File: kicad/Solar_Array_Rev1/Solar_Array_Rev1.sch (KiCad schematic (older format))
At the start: 36 parts, among them IC1 TVS_4x4, IC2 SPV1040, IC3 LTC2990.1, IC4 TVS_4x4, P1 PV_IN, P2 CONN_01X07, Q1 Q_NMOS_DGS, Q2 Q_PMOS_DGS, Q3 Q_NPN_BCE

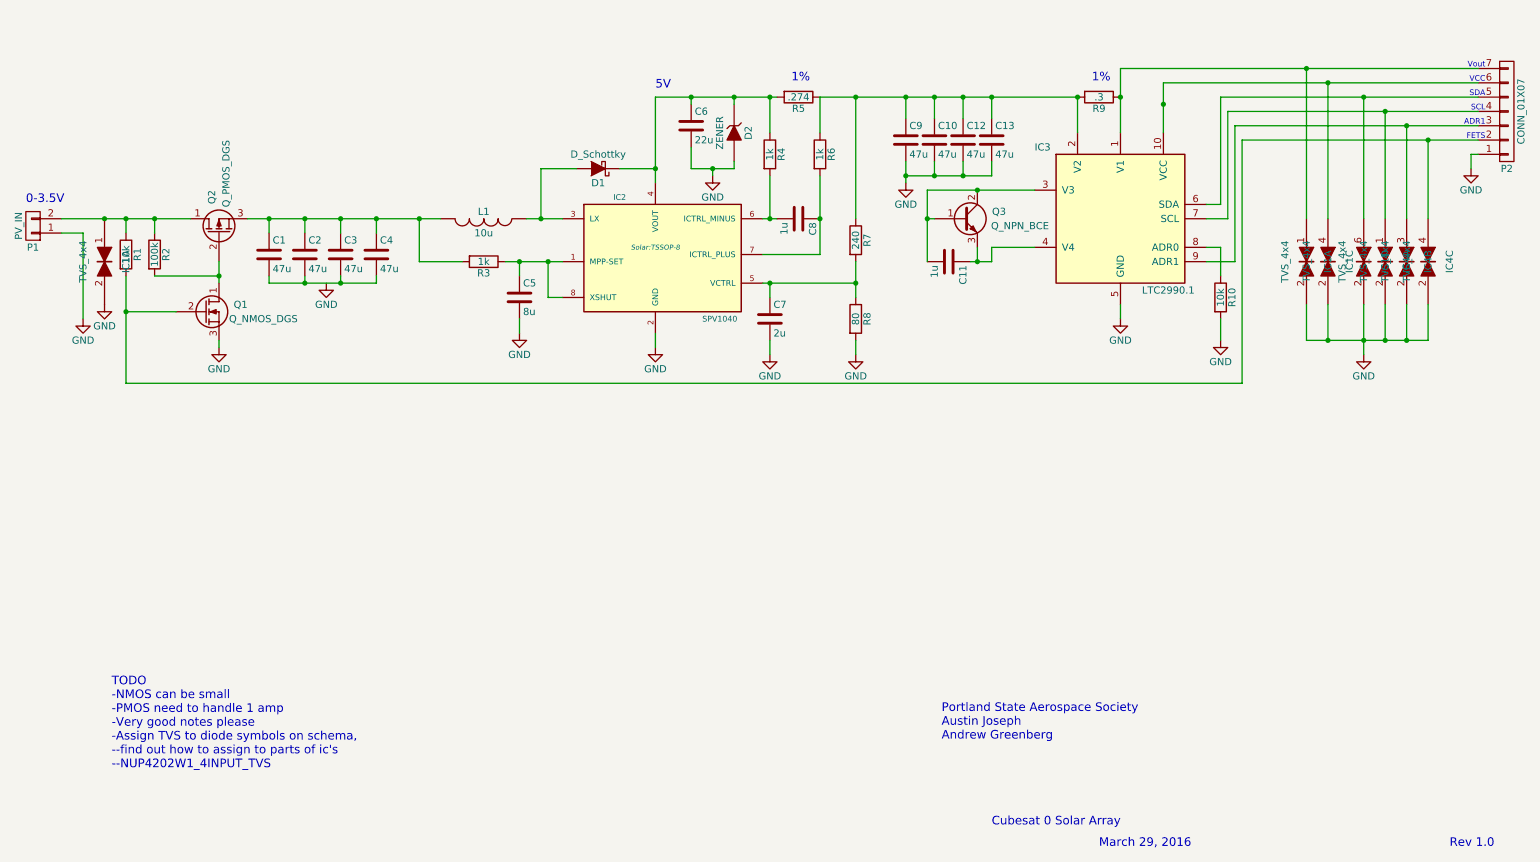
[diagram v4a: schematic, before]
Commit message: Finished Footprint/Part Selection
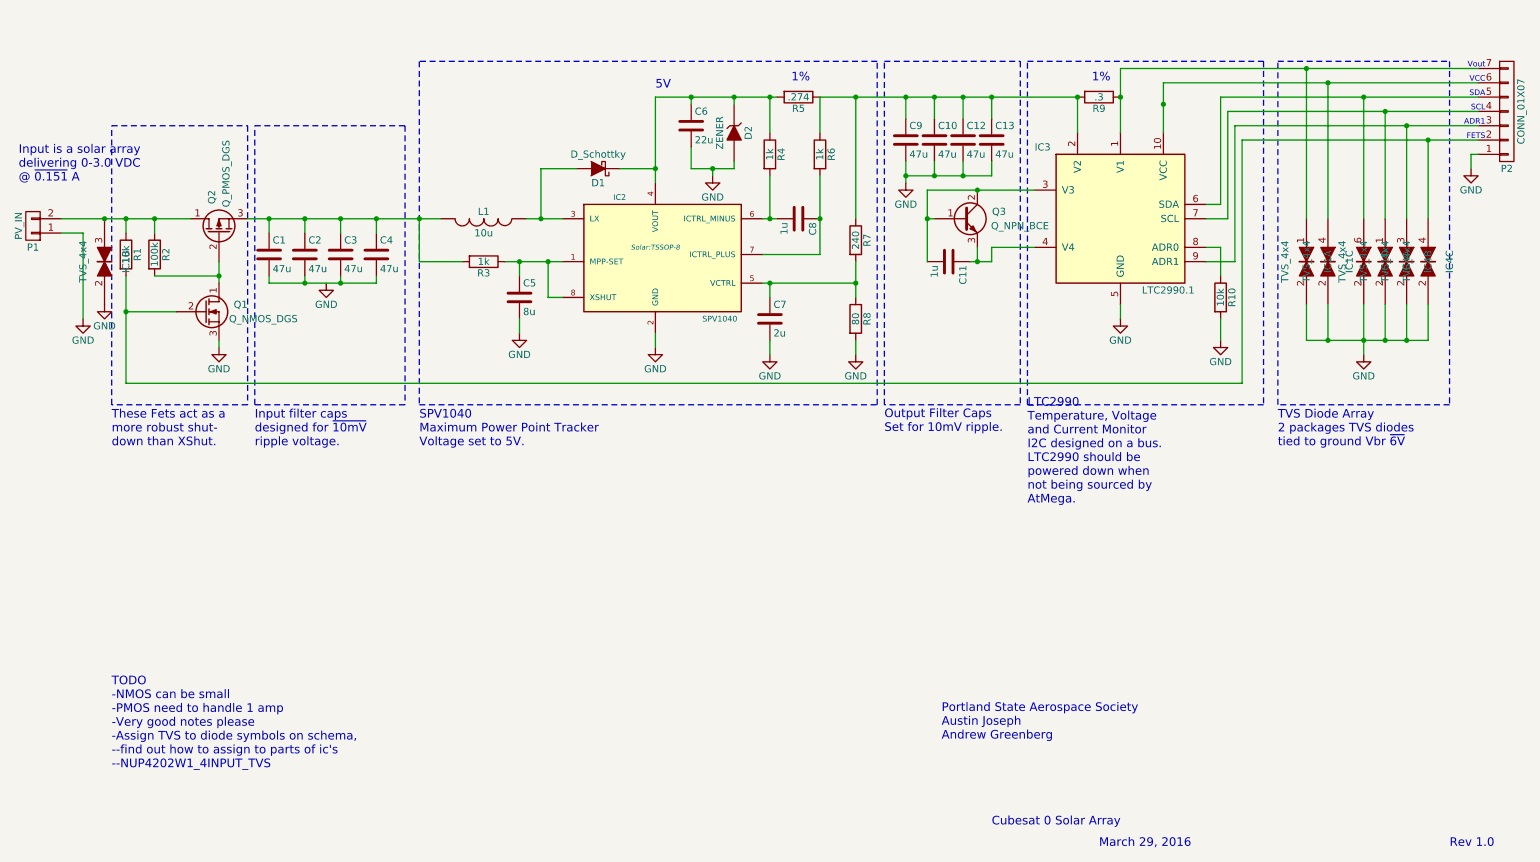
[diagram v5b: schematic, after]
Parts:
- Q1: footprint (none) -> TO_SOT_Packages_SMD:SOT-223
- Q2: footprint (none) -> TO_SOT_Packages_SMD:SOT-23
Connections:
- net at P1.2 (P2), Q2.1 (D), R1.1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: now also IC1.3; no longer IC1.1
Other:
- note added: "Input filter caps\ndesigned for ~10mV \nripple voltage."
- note added: "Input is a solar array \ndelivering 0-3.0 VDC\n@ ~0.151 A"
- note added: "LTC2990\nTemperature, Voltage\nand Current Monitor\nI2C designed on a bus.\nLTC2990 should be\npowered down when\nnot being sourced by\nAtMega."
- note added: "Output Filter Caps\nSet for 10mV ripple."
- note added: "SPV1040\nMaximum Power Point Tracker\nVoltage set to 5V."
- note added: "TVS Diode Array\n2 packages TVS diodes \ntied to ground Vbr ~6V"
- note added: "These Fets act as a\nmore robust shut-\ndown than XShut."
- note removed: "0-3.5V"
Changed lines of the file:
@@
 $EndComp
 $Comp
-L GND #PWR4
+L GND #PWR01
 U 1 1 56FC2522
 P 2750 3700
-F 0 "#PWR4" H 2750 3450 50  0001 C CNN
+F 0 "#PWR01" H 2750 3450 50  0001 C CNN
 F 1 "GND" H 2750 3550 50  0000 C CNN
 F 2 "" H 2750 3700 50  0000 C CNN
@@
 $EndComp
 $Comp
-L GND #PWR6
+L GND #PWR02
 U 1 1 56FC25A8
 P 5050 4150
-F 0 "#PWR6" H 5050 3900 50  0001 C CNN
+F 0 "#PWR02" H 5050 3900 50  0001 C CNN
 F 1 "GND" H 5050 4000 50  0000 C CNN
 F 2 "" H 5050 4150 50  0000 C CNN
@@
 $EndComp
 $Comp
-L GND #PWR5
+L GND #PWR03
 U 1 1 56FC26B3
 P 4100 4050
-F 0 "#PWR5" H 4100 3800 50  0001 C CNN
+F 0 "#PWR03" H 4100 3800 50  0001 C CNN
 F 1 "GND" H 4100 3900 50  0000 C CNN
 F 2 "" H 4100 4050 50  0000 C CNN
@@
 $EndComp
 $Comp
-L GND #PWR7
+L GND #PWR04
 U 1 1 56FC2C93
 P 5450 2950
-F 0 "#PWR7" H 5450 2700 50  0001 C CNN
+F 0 "#PWR04" H 5450 2700 50  0001 C CNN
 F 1 "GND" H 5450 2800 50  0000 C CNN
 F 2 "" H 5450 2950 50  0000 C CNN
@@
 $EndComp
 $Comp
-L GND #PWR9
+L GND #PWR05
 U 1 1 56FC2E7A
 P 6450 4200
-F 0 "#PWR9" H 6450 3950 50  0001 C CNN
+F 0 "#PWR05" H 6450 3950 50  0001 C CNN
 F 1 "GND" H 6450 4050 50  0000 C CNN
 F 2 "" H 6450 4200 50  0000 C CNN
@@
 $EndComp
 $Comp
-L GND #PWR10
+L GND #PWR06
 U 1 1 56FC34A1
 P 6800 3000
-F 0 "#PWR10" H 6800 2750 50  0001 C CNN
+F 0 "#PWR06" H 6800 2750 50  0001 C CNN
 F 1 "GND" H 6800 2850 50  0000 C CNN
 F 2 "" H 6800 3000 50  0000 C CNN
@@
 	1050 3350 1050 3950
 $Comp
-L GND #PWR1
+L GND #PWR07
 U 1 1 56FC3723
 P 1050 3950
-F 0 "#PWR1" H 1050 3700 50  0001 C CNN
+F 0 "#PWR07" H 1050 3700 50  0001 C CNN
 F 1 "GND" H 1050 3800 50  0000 C CNN
 F 2 "" H 1050 3950 50  0000 C CNN
@@
 	9050 2500 9050 3250
 $Comp
-L GND #PWR11
+L GND #PWR08
 U 1 1 56FCAF6F
 P 8300 3950
-F 0 "#PWR11" H 8300 3700 50  0001 C CNN
+F 0 "#PWR08" H 8300 3700 50  0001 C CNN
 F 1 "GND" H 8300 3800 50  0000 C CNN
 F 2 "" H 8300 3950 50  0000 C CNN
@@
 	8900 3450 9000 3450
 $Comp
-L GND #PWR12
+L GND #PWR09
 U 1 1 56FCBA35
 P 9000 4100
-F 0 "#PWR12" H 9000 3850 50  0001 C CNN
+F 0 "#PWR09" H 9000 3850 50  0001 C CNN
 F 1 "GND" H 9000 3950 50  0000 C CNN
 F 2 "" H 9000 4100 50  0000 C CNN
@@
 	9150 2700 10800 2700
 $Comp
-L GND #PWR14
+L GND #PWR010
 U 1 1 56FCEB98
 P 10750 2900
-F 0 "#PWR14" H 10750 2650 50  0001 C CNN
+F 0 "#PWR010" H 10750 2650 50  0001 C CNN
 F 1 "GND" H 10750 2750 50  0000 C CNN
 F 2 "" H 10750 2900 50  0000 C CNN
@@
 $EndComp
 $Comp
-L GND #PWR8
+L GND #PWR011
 U 1 1 56FD0196
 P 5850 4200
-F 0 "#PWR8" H 5850 3950 50  0001 C CNN
+F 0 "#PWR011" H 5850 3950 50  0001 C CNN
 F 1 "GND" H 5850 4050 50  0000 C CNN
 F 2 "" H 5850 4200 50  0000 C CNN
@@
 	6450 4100 6450 4200
 $Comp
-L GND #PWR2
+L GND #PWR012
 U 1 1 56FC80D2
 P 1200 3850
-F 0 "#PWR2" H 1200 3600 50  0001 C CNN
+F 0 "#PWR012" H 1200 3600 50  0001 C CNN
 F 1 "GND" H 1200 3700 50  0000 C CNN
 F 2 "" H 1200 3850 50  0000 C CNN
@@
 Text Notes 5050 2350 0    60   ~ 0
 5V
-Text Notes 650  3150 0    60   ~ 0
-0-3.5V
+Text Notes 600  3000 0    60   ~ 0
+Input is a solar array \ndelivering 0-3.0 VDC\n@ ~0.151 A
 Text Notes 10850 2200 2    39   ~ 0
 Vout
@@
 F 0 "Q1" H 2200 3950 50  0000 R CNN
 F 1 "Q_NMOS_DGS" H 2550 3850 50  0000 R CNN
-F 2 "" H 2100 4000 50  0001 C CNN
+F 2 "TO_SOT_Packages_SMD:SOT-223" H 2100 4000 50  0001 C CNN
 F 3 "" H 1900 3900 50  0000 C CNN
 	1    1900 3900
@@
 F 0 "Q2" H 2300 3400 50  0000 R CNN
 F 1 "Q_PMOS_DGS" H 2650 3300 50  0000 R CNN
-F 2 "" H 2200 3450 50  0001 C CNN
+F 2 "TO_SOT_Packages_SMD:SOT-23" H 2200 3450 50  0001 C CNN
 F 3 "" H 2000 3350 50  0000 C CNN
 	1    2000 3350
@@
 	2000 4100 2000 4150
 $Comp
-L GND #PWR3
+L GND #PWR013
 U 1 1 5709901A
 P 2000 4150
-F 0 "#PWR3" H 2000 3900 50  0001 C CNN
+F 0 "#PWR013" H 2000 3900 50  0001 C CNN
 F 1 "GND" H 2000 4000 50  0000 C CNN
 F 2 "" H 2000 4150 50  0000 C CNN
@@
 Connection ~ 9750 4100
 $Comp
-L GND #PWR13
+L GND #PWR014
 U 1 1 570C3955
 P 10000 4200
-F 0 "#PWR13" H 10000 3950 50  0001 C CNN
+F 0 "#PWR014" H 10000 3950 50  0001 C CNN
 F 1 "GND" H 10000 4050 50  0000 C CNN
 F 2 "" H 10000 4200 50  0000 C CNN
@@
 $Comp
 L TVS_4x4 IC1
-U 1 1 570C23EA
+U 2 1 570C23EA
 P 1200 3550
 F 0 "IC1" H 1200 3700 50  0000 C CNN
@@
 F 2 "TO_SOT_Packages_SMD:SC-70-6" H 1200 3550 50  0001 C CNN
 F 3 "" H 1200 3550 50  0000 C CNN
-	1    1200 3550
+	2    1200 3550
 	0    1    1    0
 $EndComp
@@
 	9600 3250 9600 2200
 Connection ~ 9600 2200
+Wire Notes Line
+	1250 2600 2200 2600
+Wire Notes Line
+	2200 2600 2200 4550
+Wire Notes Line
+	2200 4550 1250 4550
+Wire Notes Line
+	2250 4550 2250 2600
+Wire Notes Line
+	2250 2600 3300 2600
+Wire Notes Line
+	3300 2600 3300 4550
+Wire Notes Line
+	3300 4550 2250 4550
+Wire Notes Line
+	3400 4550 6600 4550
+Wire Notes Line
+	6600 4550 6600 2150
+Wire Notes Line
+	6600 2150 3400 2150
+Wire Notes Line
+	3400 2150 3400 4550
+Wire Notes Line
+	7650 4550 7650 2150
+Wire Notes Line
+	7650 2150 9300 2150
+Wire Notes Line
+	9300 2150 9300 4550
+Wire Notes Line
+	9300 4550 7650 4550
+Wire Notes Line
+	9400 4550 9400 2150
+Wire Notes Line
+	9400 2150 10600 2150
+Wire Notes Line
+	10600 2150 10600 4550
+Wire Notes Line
+	10600 4550 9400 4550
+Wire Notes Line
+	6650 2150 7600 2150
+Wire Notes Line
+	7600 2150 7600 4550
+Wire Notes Line
+	7600 4550 6650 4550
+Wire Notes Line
+	6650 4550 6650 2150
+Text Notes 1250 4850 0    60   ~ 0
+These Fets act as a\nmore robust shut-\ndown than XShut.
+Wire Notes Line
+	1250 4550 1250 2600
+Text Notes 2250 4850 0    60   ~ 0
+Input filter caps\ndesigned for ~10mV \nripple voltage.
+Text Notes 3400 4850 0    60   ~ 0
+SPV1040\nMaximum Power Point Tracker\nVoltage set to 5V.
+Text Notes 6650 4750 0    60   ~ 0
+Output Filter Caps\nSet for 10mV ripple.
+Text Notes 7650 5250 0    60   ~ 0
+LTC2990\nTemperature, Voltage\nand Current Monitor\nI2C designed on a bus.\nLTC2990 should be\npowered down when\nnot being sourced by\nAtMega.
+Text Notes 9400 4850 0    60   ~ 0
+TVS Diode Array\n2 packages TVS diodes \ntied to ground Vbr ~6V
 $EndSCHEMATC

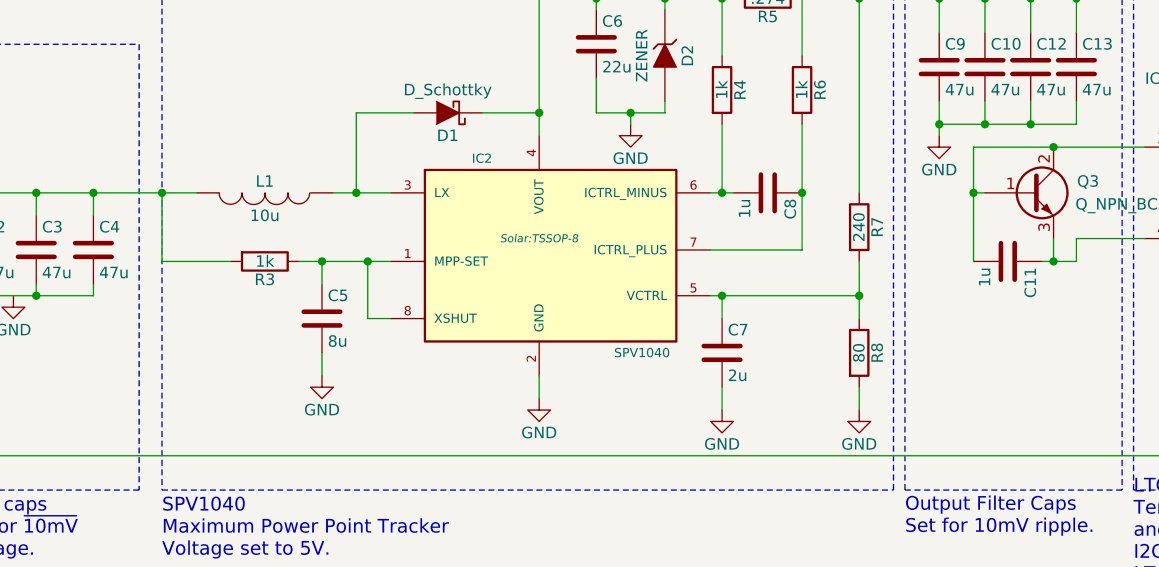
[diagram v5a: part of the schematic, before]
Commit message: Added components, updated BOM -Added parallel filter cap input. -Updated BOM to reflect new parts.
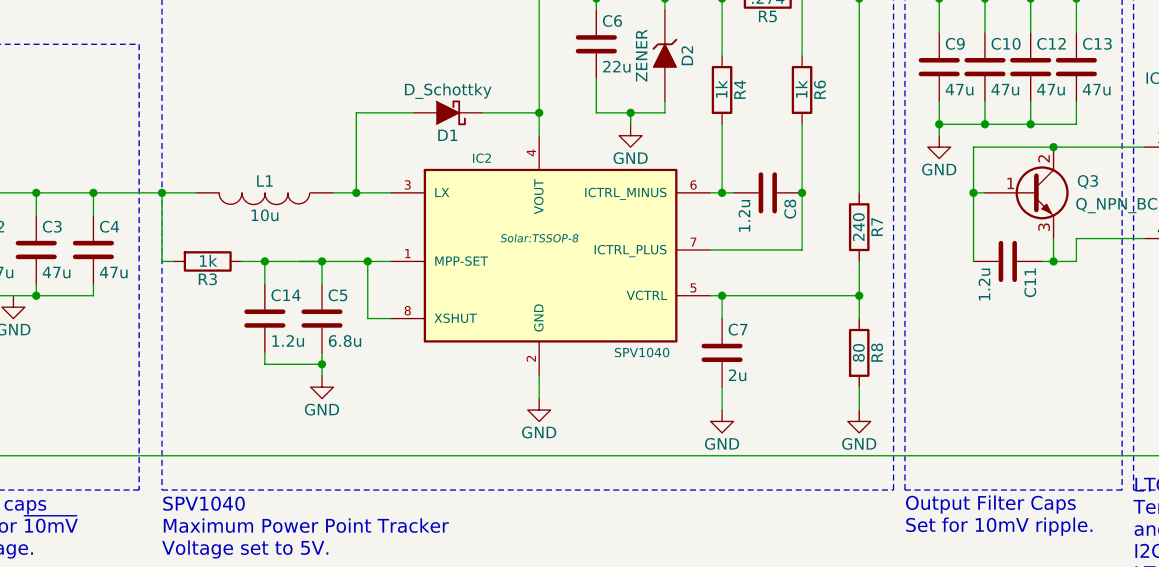
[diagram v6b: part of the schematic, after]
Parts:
- added C14: 1.2u, Capacitors_SMD:C_0603, symbol C
- C11, C8: value 1u -> 1.2u
- C5: value 8u -> 6.8u
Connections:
- net GND: now also C14.2
- net at C5.1, IC2.1 (MPP-SET), IC2.8 (XSHUT)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: now also C14.1
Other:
- moved on the sheet: R3
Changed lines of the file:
@@
 L R R3
 U 1 1 56FC2320
-P 3850 3550
-F 0 "R3" V 3930 3550 50  0000 C CNN
-F 1 "1k" V 3850 3550 50  0000 C CNN
-F 2 "Resistors_SMD:R_0603" V 3780 3550 50  0001 C CNN
-F 3 "" H 3850 3550 50  0000 C CNN
-	1    3850 3550
+P 3600 3550
+F 0 "R3" V 3680 3550 50  0000 C CNN
+F 1 "1k" V 3600 3550 50  0000 C CNN
+F 2 "Resistors_SMD:R_0603" V 3530 3550 50  0001 C CNN
+F 3 "" H 3600 3550 50  0000 C CNN
+	1    3600 3550
 	0    1    1    0
 $EndComp
@@
 $EndComp
 $Comp
-L GND #PWR01
+L GND #PWR4
 U 1 1 56FC2522
 P 2750 3700
-F 0 "#PWR01" H 2750 3450 50  0001 C CNN
+F 0 "#PWR4" H 2750 3450 50  0001 C CNN
 F 1 "GND" H 2750 3550 50  0000 C CNN
 F 2 "" H 2750 3700 50  0000 C CNN
@@
 $EndComp
 $Comp
-L GND #PWR02
+L GND #PWR6
 U 1 1 56FC25A8
 P 5050 4150
-F 0 "#PWR02" H 5050 3900 50  0001 C CNN
+F 0 "#PWR6" H 5050 3900 50  0001 C CNN
 F 1 "GND" H 5050 4000 50  0000 C CNN
 F 2 "" H 5050 4150 50  0000 C CNN
@@
 P 4100 3800
 F 0 "C5" H 4125 3900 50  0000 L CNN
-F 1 "8u" H 4125 3700 50  0000 L CNN
+F 1 "6.8u" H 4125 3700 50  0000 L CNN
 F 2 "Capacitors_SMD:C_0603" H 4138 3650 50  0001 C CNN
 F 3 "" H 4100 3800 50  0000 C CNN
@@
 $EndComp
 $Comp
-L GND #PWR03
+L GND #PWR5
 U 1 1 56FC26B3
 P 4100 4050
-F 0 "#PWR03" H 4100 3800 50  0001 C CNN
+F 0 "#PWR5" H 4100 3800 50  0001 C CNN
 F 1 "GND" H 4100 3900 50  0000 C CNN
 F 2 "" H 4100 4050 50  0000 C CNN
@@
 P 6050 3250
 F 0 "C8" H 6075 3350 50  0000 L CNN
-F 1 "1u" H 6075 3150 50  0000 L CNN
+F 1 "1.2u" H 6075 3150 50  0000 L CNN
 F 2 "Capacitors_SMD:C_0603" H 6088 3100 50  0001 C CNN
 F 3 "" H 6050 3250 50  0000 C CNN
@@
 $EndComp
 $Comp
-L GND #PWR04
+L GND #PWR7
 U 1 1 56FC2C93
 P 5450 2950
-F 0 "#PWR04" H 5450 2700 50  0001 C CNN
+F 0 "#PWR7" H 5450 2700 50  0001 C CNN
 F 1 "GND" H 5450 2800 50  0000 C CNN
 F 2 "" H 5450 2950 50  0000 C CNN
@@
 $EndComp
 $Comp
-L GND #PWR05
+L GND #PWR9
 U 1 1 56FC2E7A
 P 6450 4200
-F 0 "#PWR05" H 6450 3950 50  0001 C CNN
+F 0 "#PWR9" H 6450 3950 50  0001 C CNN
 F 1 "GND" H 6450 4050 50  0000 C CNN
 F 2 "" H 6450 4200 50  0000 C CNN
@@
 	5050 2400 5050 3000
 Connection ~ 5050 2900
-Wire Wire Line
-	3400 3550 3700 3550
 Connection ~ 2850 3250
 Wire Wire Line
@@
 $EndComp
 $Comp
-L GND #PWR06
+L GND #PWR10
 U 1 1 56FC34A1
 P 6800 3000
-F 0 "#PWR06" H 6800 2750 50  0001 C CNN
+F 0 "#PWR10" H 6800 2750 50  0001 C CNN
 F 1 "GND" H 6800 2850 50  0000 C CNN
 F 2 "" H 6800 3000 50  0000 C CNN
@@
 	1050 3350 1050 3950
 $Comp
-L GND #PWR07
+L GND #PWR1
 U 1 1 56FC3723
 P 1050 3950
-F 0 "#PWR07" H 1050 3700 50  0001 C CNN
+F 0 "#PWR1" H 1050 3700 50  0001 C CNN
 F 1 "GND" H 1050 3800 50  0000 C CNN
 F 2 "" H 1050 3950 50  0000 C CNN
@@
 P 7100 3550
 F 0 "C11" H 7125 3650 50  0000 L CNN
-F 1 "1u" H 7125 3450 50  0000 L CNN
+F 1 "1.2u" H 7125 3450 50  0000 L CNN
 F 2 "Capacitors_SMD:C_0603" H 7138 3400 50  0001 C CNN
 F 3 "" H 7100 3550 50  0000 C CNN
@@
 	9050 2500 9050 3250
 $Comp
-L GND #PWR08
+L GND #PWR11
 U 1 1 56FCAF6F
 P 8300 3950
-F 0 "#PWR08" H 8300 3700 50  0001 C CNN
+F 0 "#PWR11" H 8300 3700 50  0001 C CNN
 F 1 "GND" H 8300 3800 50  0000 C CNN
 F 2 "" H 8300 3950 50  0000 C CNN
@@
 	8900 3450 9000 3450
 $Comp
-L GND #PWR09
+L GND #PWR12
 U 1 1 56FCBA35
 P 9000 4100
-F 0 "#PWR09" H 9000 3850 50  0001 C CNN
+F 0 "#PWR12" H 9000 3850 50  0001 C CNN
 F 1 "GND" H 9000 3950 50  0000 C CNN
 F 2 "" H 9000 4100 50  0000 C CNN
@@
 	9150 2700 10800 2700
 $Comp
-L GND #PWR010
+L GND #PWR14
 U 1 1 56FCEB98
 P 10750 2900
-F 0 "#PWR010" H 10750 2650 50  0001 C CNN
+F 0 "#PWR14" H 10750 2650 50  0001 C CNN
 F 1 "GND" H 10750 2750 50  0000 C CNN
 F 2 "" H 10750 2900 50  0000 C CNN
@@
 $EndComp
 $Comp
-L GND #PWR011
+L GND #PWR8
 U 1 1 56FD0196
 P 5850 4200
-F 0 "#PWR011" H 5850 3950 50  0001 C CNN
+F 0 "#PWR8" H 5850 3950 50  0001 C CNN
 F 1 "GND" H 5850 4050 50  0000 C CNN
 F 2 "" H 5850 4200 50  0000 C CNN
@@
 	6450 4100 6450 4200
 $Comp
-L GND #PWR012
+L GND #PWR2
 U 1 1 56FC80D2
 P 1200 3850
-F 0 "#PWR012" H 1200 3600 50  0001 C CNN
+F 0 "#PWR2" H 1200 3600 50  0001 C CNN
 F 1 "GND" H 1200 3700 50  0000 C CNN
 F 2 "" H 1200 3850 50  0000 C CNN
@@
 	2000 4100 2000 4150
 $Comp
-L GND #PWR013
+L GND #PWR3
 U 1 1 5709901A
 P 2000 4150
-F 0 "#PWR013" H 2000 3900 50  0001 C CNN
+F 0 "#PWR3" H 2000 3900 50  0001 C CNN
 F 1 "GND" H 2000 4000 50  0000 C CNN
 F 2 "" H 2000 4150 50  0000 C CNN
@@
 Connection ~ 9750 4100
 $Comp
-L GND #PWR014
+L GND #PWR13
 U 1 1 570C3955
 P 10000 4200
-F 0 "#PWR014" H 10000 3950 50  0001 C CNN
+F 0 "#PWR13" H 10000 3950 50  0001 C CNN
 F 1 "GND" H 10000 4050 50  0000 C CNN
 F 2 "" H 10000 4200 50  0000 C CNN
@@
 Text Notes 9400 4850 0    60   ~ 0
 TVS Diode Array\n2 packages TVS diodes \ntied to ground Vbr ~6V
+Wire Wire Line
+	3400 3550 3450 3550
+$Comp
+L C C14
+U 1 1 570D89CF
+P 3850 3800
+F 0 "C14" H 3875 3900 50  0000 L CNN
+F 1 "1.2u" H 3875 3700 50  0000 L CNN
+F 2 "Capacitors_SMD:C_0603" H 3888 3650 50  0001 C CNN
+F 3 "" H 3850 3800 50  0000 C CNN
+	1    3850 3800
+	1    0    0    -1
+$EndComp
+Wire Wire Line
+	4100 3550 3750 3550
+Wire Wire Line
+	3850 3650 3850 3550
+Connection ~ 3850 3550
+Wire Wire Line
+	3850 3950 3850 4000
+Wire Wire Line
+	3850 4000 4100 4000
+Connection ~ 4100 4000
 $EndSCHEMATC
